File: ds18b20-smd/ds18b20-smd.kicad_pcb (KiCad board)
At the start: 2 copper layers, 4 parts, among them U1 DS18B20Z

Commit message: update project
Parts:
- removed H1, H2, H3: MountingHole_Pad, project_footprints:CONN_01x01_PAD
- added DQ1: Pad, project_footprints:PAD, B.Cu at (95.2, 100.1)
- added GND1: Pad, project_footprints:PAD, B.Cu at (102.6, 100.1)
- added VCC1: Pad, project_footprints:PAD, F.Cu at (93.0, 100.1)
- moved U1 44.4 mm to (100.1, 100.1)
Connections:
- U1 pad 3: VCC -> (no net)
- U1 pad 4: DQ -> (no net)
- U1 pad 5: GND -> (no net)
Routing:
- net GND: track 21.8 -> 0.00 mm, vias 2 -> 0
- net VCC: track 7.00 -> 0.00 mm
- net DQ: track 6.56 -> 0.00 mm
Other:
- board outline added: 13.7 x 6.1 mm
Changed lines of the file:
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@@
   (general
     (thickness 1.6)
-    (drawings 0)
-    (tracks 15)
+    (drawings 10)
+    (tracks 0)
     (zones 0)
     (modules 4)
-    (nets 4)
+    (nets 1)
   )
   (page A4)
@@
     (mod_text_size 1 1)
     (mod_text_width 0.15)
-    (pad_size 1.524 1.524)
-    (pad_drill 0.762)
+    (pad_size 5 3)
+    (pad_drill 0)
     (pad_to_mask_clearance 0.051)
     (solder_mask_min_width 0.25)
@@
   )
   (net 0 "")
-  (net 1 VCC)
-  (net 2 DQ)
-  (net 3 GND)
   (net_class Default "This is the default net class."
     (clearance 0.2)
@@
     (uvia_dia 0.3)
     (uvia_drill 0.1)
-    (add_net DQ)
-    (add_net GND)
-    (add_net VCC)
-  )
-  (module project_footprints:CONN_01x01_PAD (layer F.Cu)
-    (at 134.6708 97.4344 270)
-    (fp_text reference H1 (at 0 2.54 270) (layer F.SilkS)
-      (effects (font (size 1 1) (thickness 0.15)))
-    )
-    (fp_text value MountingHole_Pad (at 0 -0.5 270) (layer F.Fab) hide
-      (effects (font (size 1 1) (thickness 0.15)))
-    )
-    (pad 1 thru_hole circle (at 0 0 270) (size 1.75 1.75) (drill 0.75) (layers *.Cu *.Mask F.SilkS)
-      (net 1 VCC))
-  )
-  (module project_footprints:CONN_01x01_PAD (layer F.Cu)
-    (at 134.6708 99.8728 270)
-    (fp_text reference H2 (at 0 2.54 270) (layer F.SilkS)
-      (effects (font (size 1 1) (thickness 0.15)))
-    )
-    (fp_text value MountingHole_Pad (at 0 -0.5 270) (layer F.Fab) hide
-      (effects (font (size 1 1) (thickness 0.15)))
-    )
-    (pad 1 thru_hole circle (at 0 0 270) (size 1.75 1.75) (drill 0.75) (layers *.Cu *.Mask F.SilkS)
-      (net 2 DQ))
-  )
-  (module project_footprints:CONN_01x01_PAD (layer F.Cu)
-    (at 134.7216 94.8436 270)
-    (fp_text reference H3 (at 0 2.54 270) (layer F.SilkS)
-      (effects (font (size 1 1) (thickness 0.15)))
-    )
-    (fp_text value MountingHole_Pad (at 0 -0.5 270) (layer F.Fab) hide
-      (effects (font (size 1 1) (thickness 0.15)))
-    )
-    (pad 1 thru_hole circle (at 0 0 270) (size 1.75 1.75) (drill 0.75) (layers *.Cu *.Mask F.SilkS)
-      (net 3 GND))
   )
   (module "kicad-gfa local:SOIC-8-N" (layer F.Cu)
-    (at 144.3863 97.915801 270)
+    (at 100.076 100.076 270)
     (descr "Module Narrow CMS SOJ 8 pins large")
     (tags "CMS SOJ")
     (attr smd)
-    (fp_text reference U1 (at -3.462 0.136) (layer F.SilkS)
+    (fp_text reference U1 (at 0.076 -0.076) (layer F.SilkS)
       (effects (font (size 1 1) (thickness 0.15)))
     )
@@
     (pad 7 smd rect (at -0.635 -3.175 270) (size 0.508 1.143) (layers F.Cu F.Paste F.Mask))
     (pad 6 smd rect (at 0.635 -3.175 270) (size 0.508 1.143) (layers F.Cu F.Paste F.Mask))
-    (pad 5 smd rect (at 1.905 -3.175 270) (size 0.508 1.143) (layers F.Cu F.Paste F.Mask)
-      (net 3 GND))
-    (pad 4 smd rect (at 1.905 3.175 270) (size 0.508 1.143) (layers F.Cu F.Paste F.Mask)
-      (net 2 DQ))
-    (pad 3 smd rect (at 0.635 3.175 270) (size 0.508 1.143) (layers F.Cu F.Paste F.Mask)
-      (net 1 VCC))
+    (pad 5 smd rect (at 1.905 -3.175 270) (size 0.508 1.143) (layers F.Cu F.Paste F.Mask))
+    (pad 4 smd rect (at 1.905 3.175 270) (size 0.508 1.143) (layers F.Cu F.Paste F.Mask))
+    (pad 3 smd rect (at 0.635 3.175 270) (size 0.508 1.143) (layers F.Cu F.Paste F.Mask))
     (pad 2 smd rect (at -0.635 3.175 270) (size 0.508 1.143) (layers F.Cu F.Paste F.Mask))
     (pad 1 smd rect (at -1.905 3.175 270) (size 0.508 1.143) (layers F.Cu F.Paste F.Mask))
@@
     )
   )
-  (segment (start 140.3898 98.550801) (end 141.2113 98.550801) (width 0.25) (layer F.Cu) (net 1) (status 20))
-  (segment (start 137.024637 98.550801) (end 140.3898 98.550801) (width 0.25) (layer F.Cu) (net 1))
-  (segment (start 135.908236 97.4344) (end 137.024637 98.550801) (width 0.25) (layer F.Cu) (net 1))
-  (segment (start 134.6708 97.4344) (end 135.908236 97.4344) (width 0.25) (layer F.Cu) (net 1) (status 10))
-  (segment (start 141.159301 99.8728) (end 141.2113 99.820801) (width 0.25) (layer F.Cu) (net 2) (status 30))
-  (segment (start 134.6708 99.8728) (end 141.159301 99.8728) (width 0.25) (layer F.Cu) (net 2) (status 30))
-  (via (at 136.5504 94.8436) (size 0.8) (drill 0.4) (layers F.Cu B.Cu) (net 3))
-  (segment (start 134.7216 94.8436) (end 136.5504 94.8436) (width 0.25) (layer F.Cu) (net 3) (status 10))
-  (segment (start 136.5504 94.8436) (end 138.9888 97.282) (width 0.25) (layer B.Cu) (net 3))
-  (segment (start 138.9888 97.282) (end 150.0632 97.282) (width 0.25) (layer B.Cu) (net 3))
-  (segment (start 150.0632 97.282) (end 150.1648 97.3836) (width 0.25) (layer B.Cu) (net 3))
-  (via (at 150.1648 100.0252) (size 0.8) (drill 0.4) (layers F.Cu B.Cu) (net 3))
-  (segment (start 150.1648 97.3836) (end 150.1648 100.0252) (width 0.25) (layer B.Cu) (net 3))
-  (segment (start 147.765699 100.0252) (end 147.5613 99.820801) (width 0.25) (layer F.Cu) (net 3) (status 30))
-  (segment (start 150.1648 100.0252) (end 147.765699 100.0252) (width 0.25) (layer F.Cu) (net 3) (status 20))
+  (module project_footprints:PAD (layer B.Cu)
+    (at 95.25 100.076 90)
+    (attr smd)
+    (fp_text reference DQ1 (at 0 2.504 -90) (layer B.SilkS)
+      (effects (font (size 1 1) (thickness 0.15)) (justify mirror))
+    )
+    (fp_text value Pad (at 0 2.54 90) (layer B.Fab) hide
+      (effects (font (size 1 1) (thickness 0.15)) (justify mirror))
+    )
+    (pad "" smd roundrect (at 0 0 90) (size 5 3) (layers B.Cu B.Paste B.Mask) (roundrect_rratio 0.25))
+  )
+  (module project_footprints:PAD (layer B.Cu)
+    (at 102.616 100.076 90)
+    (attr smd)
+    (fp_text reference GND1 (at 0 -2.54 90) (layer B.SilkS)
+      (effects (font (size 1 1) (thickness 0.15)) (justify mirror))
+    )
+    (fp_text value Pad (at 0 2.54 90) (layer B.Fab) hide
+      (effects (font (size 1 1) (thickness 0.15)) (justify mirror))
+    )
+    (pad "" smd roundrect (at 0 0 90) (size 5 3) (layers B.Cu B.Paste B.Mask) (roundrect_rratio 0.25))
+  )
+  (module project_footprints:PAD (layer F.Cu)
+    (at 92.964 100.076 90)
+    (attr smd)
+    (fp_text reference VCC1 (at 0 2.54 90) (layer F.SilkS)
+      (effects (font (size 1 1) (thickness 0.15)))
+    )
+    (fp_text value Pad (at 0 -2.54 90) (layer F.Fab) hide
+      (effects (font (size 1 1) (thickness 0.15)))
+    )
+    (pad "" smd roundrect (at 0 0 90) (size 5 3) (layers F.Cu F.Paste F.Mask) (roundrect_rratio 0.25))
+  )
+  (dimension 6.096 (width 0.3) (layer Dwgs.User)
+    (gr_text "6.096 mm" (at 111.32 100.076 270) (layer Dwgs.User)
+      (effects (font (size 1.5 1.5) (thickness 0.3)))
+    )
+    (feature1 (pts (xy 101.854 103.124) (xy 109.806421 103.124)))
+    (feature2 (pts (xy 101.854 97.028) (xy 109.806421 97.028)))
+    (crossbar (pts (xy 109.22 97.028) (xy 109.22 103.124)))
+    (arrow1a (pts (xy 109.22 103.124) (xy 108.633579 101.997496)))
+    (arrow1b (pts (xy 109.22 103.124) (xy 109.806421 101.997496)))
+    (arrow2a (pts (xy 109.22 97.028) (xy 108.633579 98.154504)))
+    (arrow2b (pts (xy 109.22 97.028) (xy 109.806421 98.154504)))
+  )
+  (dimension 13.716 (width 0.3) (layer Dwgs.User)
+    (gr_text "13.716 mm" (at 97.79 108.018) (layer Dwgs.User)
+      (effects (font (size 1.5 1.5) (thickness 0.3)))
+    )
+    (feature1 (pts (xy 104.648 101.092) (xy 104.648 106.504421)))
+    (feature2 (pts (xy 90.932 101.092) (xy 90.932 106.504421)))
+    (crossbar (pts (xy 90.932 105.918) (xy 104.648 105.918)))
+    (arrow1a (pts (xy 104.648 105.918) (xy 103.521496 106.504421)))
+    (arrow1b (pts (xy 104.648 105.918) (xy 103.521496 105.331579)))
+    (arrow2a (pts (xy 90.932 105.918) (xy 92.058504 106.504421)))
+    (arrow2b (pts (xy 90.932 105.918) (xy 92.058504 105.331579)))
+  )
+  (gr_line (start 90.932 98.298) (end 90.932 101.854) (layer Edge.Cuts) (width 0.15))
+  (gr_line (start 104.648 98.298) (end 104.648 101.854) (layer Edge.Cuts) (width 0.15))
+  (gr_line (start 103.378 103.124) (end 92.202 103.124) (layer Edge.Cuts) (width 0.15))
+  (gr_line (start 103.378 97.028) (end 92.202 97.028) (layer Edge.Cuts) (width 0.15))
+  (gr_arc (start 103.378 98.298) (end 104.648 98.298) (angle -90) (layer Edge.Cuts) (width 0.15))
+  (gr_arc (start 103.378 101.854) (end 103.378 103.124) (angle -90) (layer Edge.Cuts) (width 0.15))
+  (gr_arc (start 92.202 101.854) (end 90.932 101.854) (angle -90) (layer Edge.Cuts) (width 0.15))
+  (gr_arc (start 92.202 98.298) (end 92.202 97.028) (angle -90) (layer Edge.Cuts) (width 0.15))
 )

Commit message: ready for release
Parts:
- DQ1, GND1, VCC1: footprint project_footprints:PAD -> project_footprints:PAD3mmx5mm
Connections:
- U1 pad 3: (no net) -> VCC
- U1 pad 4: (no net) -> DQ
- U1 pad 5: (no net) -> GND
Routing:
- net GND: track 0.00 -> 7.55 mm, vias 0 -> 1
- net DQ: track 0.00 -> 6.66 mm, vias 0 -> 1
- net VCC: track 0.00 -> 4.22 mm
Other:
- board text added: "UMONS-GFA 2018-11"
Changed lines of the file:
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@@
   (general
     (thickness 1.6)
-    (drawings 10)
-    (tracks 0)
+    (drawings 11)
+    (tracks 15)
     (zones 0)
     (modules 4)
-    (nets 1)
+    (nets 4)
   )
   (page A4)
@@
     (35 F.Paste user)
     (36 B.SilkS user)
-    (37 F.SilkS user)
+    (37 F.SilkS user hide)
     (38 B.Mask user)
     (39 F.Mask user)
@@
     (46 B.CrtYd user)
     (47 F.CrtYd user)
-    (48 B.Fab user)
+    (48 B.Fab user hide)
     (49 F.Fab user)
   )
@@
   )
   (net 0 "")
+  (net 1 DQ)
+  (net 2 GND)
+  (net 3 VCC)
   (net_class Default "This is the default net class."
     (clearance 0.2)
@@
     (uvia_dia 0.3)
     (uvia_drill 0.1)
+    (add_net DQ)
+    (add_net GND)
+    (add_net VCC)
   )
   (module "kicad-gfa local:SOIC-8-N" (layer F.Cu)
@@
     (pad 7 smd rect (at -0.635 -3.175 270) (size 0.508 1.143) (layers F.Cu F.Paste F.Mask))
     (pad 6 smd rect (at 0.635 -3.175 270) (size 0.508 1.143) (layers F.Cu F.Paste F.Mask))
-    (pad 5 smd rect (at 1.905 -3.175 270) (size 0.508 1.143) (layers F.Cu F.Paste F.Mask))
-    (pad 4 smd rect (at 1.905 3.175 270) (size 0.508 1.143) (layers F.Cu F.Paste F.Mask))
-    (pad 3 smd rect (at 0.635 3.175 270) (size 0.508 1.143) (layers F.Cu F.Paste F.Mask))
+    (pad 5 smd rect (at 1.905 -3.175 270) (size 0.508 1.143) (layers F.Cu F.Paste F.Mask)
+      (net 2 GND))
+    (pad 4 smd rect (at 1.905 3.175 270) (size 0.508 1.143) (layers F.Cu F.Paste F.Mask)
+      (net 1 DQ))
+    (pad 3 smd rect (at 0.635 3.175 270) (size 0.508 1.143) (layers F.Cu F.Paste F.Mask)
+      (net 3 VCC))
     (pad 2 smd rect (at -0.635 3.175 270) (size 0.508 1.143) (layers F.Cu F.Paste F.Mask))
     (pad 1 smd rect (at -1.905 3.175 270) (size 0.508 1.143) (layers F.Cu F.Paste F.Mask))
@@
     )
   )
-  (module project_footprints:PAD (layer B.Cu)
+  (module project_footprints:PAD3mmx5mm (layer B.Cu)
     (at 95.25 100.076 90)
-    (attr smd)
-    (fp_text reference DQ1 (at 0 2.504 -90) (layer B.SilkS)
-      (effects (font (size 1 1) (thickness 0.15)) (justify mirror))
-    )
-    (fp_text value Pad (at 0 2.54 90) (layer B.Fab) hide
-      (effects (font (size 1 1) (thickness 0.15)) (justify mirror))
-    )
-    (pad "" smd roundrect (at 0 0 90) (size 5 3) (layers B.Cu B.Paste B.Mask) (roundrect_rratio 0.25))
-  )
-  (module project_footprints:PAD (layer B.Cu)
+    (fp_text reference DQ1 (at 0 -2.54 90) (layer B.SilkS)
+      (effects (font (size 1 1) (thickness 0.15)) (justify mirror))
+    )
+    (fp_text value Pad (at 0 2.54 90) (layer B.Fab)
+      (effects (font (size 1 1) (thickness 0.15)) (justify mirror))
+    )
+    (pad 1 smd roundrect (at 0 0 90) (size 5 3) (layers B.Cu B.Paste B.Mask) (roundrect_rratio 0.25)
+      (net 1 DQ))
+  )
+  (module project_footprints:PAD3mmx5mm (layer B.Cu)
     (at 102.616 100.076 90)
-    (attr smd)
     (fp_text reference GND1 (at 0 -2.54 90) (layer B.SilkS)
       (effects (font (size 1 1) (thickness 0.15)) (justify mirror))
     )
-    (fp_text value Pad (at 0 2.54 90) (layer B.Fab) hide
-      (effects (font (size 1 1) (thickness 0.15)) (justify mirror))
-    )
-    (pad "" smd roundrect (at 0 0 90) (size 5 3) (layers B.Cu B.Paste B.Mask) (roundrect_rratio 0.25))
-  )
-  (module project_footprints:PAD (layer F.Cu)
+    (fp_text value Pad (at 0 2.54 90) (layer B.Fab)
+      (effects (font (size 1 1) (thickness 0.15)) (justify mirror))
+    )
+    (pad 1 smd roundrect (at 0 0 90) (size 5 3) (layers B.Cu B.Paste B.Mask) (roundrect_rratio 0.25)
+      (net 2 GND))
+  )
+  (module project_footprints:PAD3mmx5mm (layer F.Cu)
     (at 92.964 100.076 90)
-    (attr smd)
     (fp_text reference VCC1 (at 0 2.54 90) (layer F.SilkS)
       (effects (font (size 1 1) (thickness 0.15)))
     )
-    (fp_text value Pad (at 0 -2.54 90) (layer F.Fab) hide
-      (effects (font (size 1 1) (thickness 0.15)))
-    )
-    (pad "" smd roundrect (at 0 0 90) (size 5 3) (layers F.Cu F.Paste F.Mask) (roundrect_rratio 0.25))
+    (fp_text value Pad (at 0 -2.54 90) (layer F.Fab)
+      (effects (font (size 1 1) (thickness 0.15)))
+    )
+    (pad 1 smd roundrect (at 0 0 90) (size 5 3) (layers F.Cu F.Paste F.Mask) (roundrect_rratio 0.25)
+      (net 3 VCC))
+  )
+  (gr_text "UMONS-GFA\n2018-11" (at 97.8408 100.1776 90) (layer B.SilkS)
+    (effects (font (size 0.5 0.5) (thickness 0.125)) (justify mirror))
   )
   (dimension 6.096 (width 0.3) (layer Dwgs.User)
@@
   (gr_arc (start 92.202 101.854) (end 90.932 101.854) (angle -90) (layer Edge.Cuts) (width 0.15))
   (gr_arc (start 92.202 98.298) (end 92.202 97.028) (angle -90) (layer Edge.Cuts) (width 0.15))
+  (via (at 99.0092 101.9048) (size 0.8) (drill 0.4) (layers F.Cu B.Cu) (net 1))
+  (segment (start 95.25 100.076) (end 97.1804 100.076) (width 0.25) (layer B.Cu) (net 1))
+  (segment (start 97.1804 100.076) (end 99.0092 101.9048) (width 0.25) (layer B.Cu) (net 1))
+  (segment (start 96.9772 101.9048) (end 96.901 101.981) (width 0.25) (layer F.Cu) (net 1))
+  (segment (start 99.0092 101.9048) (end 96.9772 101.9048) (width 0.25) (layer F.Cu) (net 1))
+  (via (at 99.7204 100.076) (size 0.8) (drill 0.4) (layers F.Cu B.Cu) (net 2))
+  (segment (start 102.616 100.076) (end 99.7204 100.076) (width 0.25) (layer B.Cu) (net 2))
+  (segment (start 102.4295 101.981) (end 103.251 101.981) (width 0.25) (layer F.Cu) (net 2))
+  (segment (start 101.059715 101.981) (end 102.4295 101.981) (width 0.25) (layer F.Cu) (net 2))
+  (segment (start 99.7204 100.641685) (end 101.059715 101.981) (width 0.25) (layer F.Cu) (net 2))
+  (segment (start 99.7204 100.076) (end 99.7204 100.641685) (width 0.25) (layer F.Cu) (net 2))
+  (segment (start 94.564 100.076) (end 95.2244 100.7364) (width 0.25) (layer F.Cu) (net 3))
+  (segment (start 92.964 100.076) (end 94.564 100.076) (width 0.25) (layer F.Cu) (net 3))
+  (segment (start 95.2498 100.711) (end 96.901 100.711) (width 0.25) (layer F.Cu) (net 3))
+  (segment (start 95.2244 100.7364) (end 95.2498 100.711) (width 0.25) (layer F.Cu) (net 3))
 )

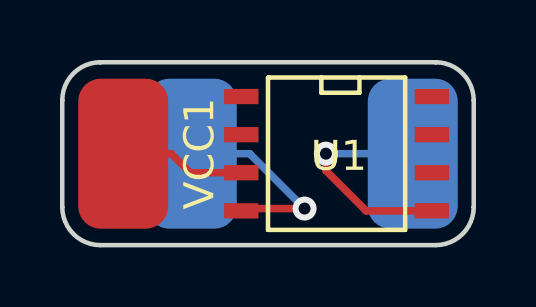
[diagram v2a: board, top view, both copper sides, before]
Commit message: add filled zones
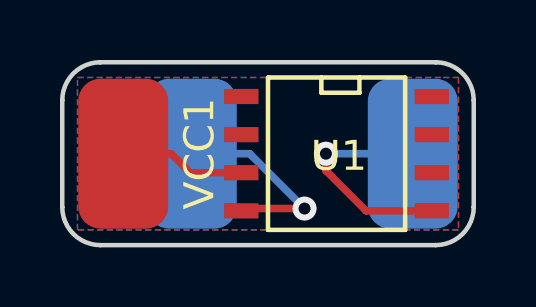
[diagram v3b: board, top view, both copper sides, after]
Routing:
- added copper zone on B.Cu, net GND
- added copper zone on F.Cu, net GND
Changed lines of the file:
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@@
       (outputformat 1)
       (mirror false)
-      (drillshape 1)
+      (drillshape 0)
       (scaleselection 1)
-      (outputdirectory ""))
+      (outputdirectory "gerber/"))
   )
   (net 0 "")
@@
   (segment (start 95.2498 100.711) (end 96.901 100.711) (width 0.25) (layer F.Cu) (net 3))
   (segment (start 95.2244 100.7364) (end 95.2498 100.711) (width 0.25) (layer F.Cu) (net 3))
+  (zone (net 2) (net_name GND) (layer F.Cu) (hatch edge 0.508)
+    (connect_pads (clearance 0.508))
+    (min_thickness 0.254)
+    (fill yes (arc_segments 16) (thermal_gap 0.508) (thermal_bridge_width 0.508))
+    (polygon
+      (pts
+        (xy 98.552 97.536) (xy 103.632 97.536) (xy 104.14 97.536) (xy 104.14 102.616) (xy 91.44 102.616)
+        (xy 91.44 97.536)
+      )
+    )
+  )
+  (zone (net 2) (net_name GND) (layer B.Cu) (hatch edge 0.508)
+    (connect_pads (clearance 0.508))
+    (min_thickness 0.254)
+    (fill yes (arc_segments 16) (thermal_gap 0.508) (thermal_bridge_width 0.508))
+    (polygon
+      (pts
+        (xy 98.552 97.536) (xy 103.632 97.536) (xy 104.14 97.536) (xy 104.14 102.616) (xy 91.44 102.616)
+        (xy 91.44 97.536)
+      )
+    )
+  )
 )
